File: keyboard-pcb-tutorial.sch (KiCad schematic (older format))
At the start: 14 parts

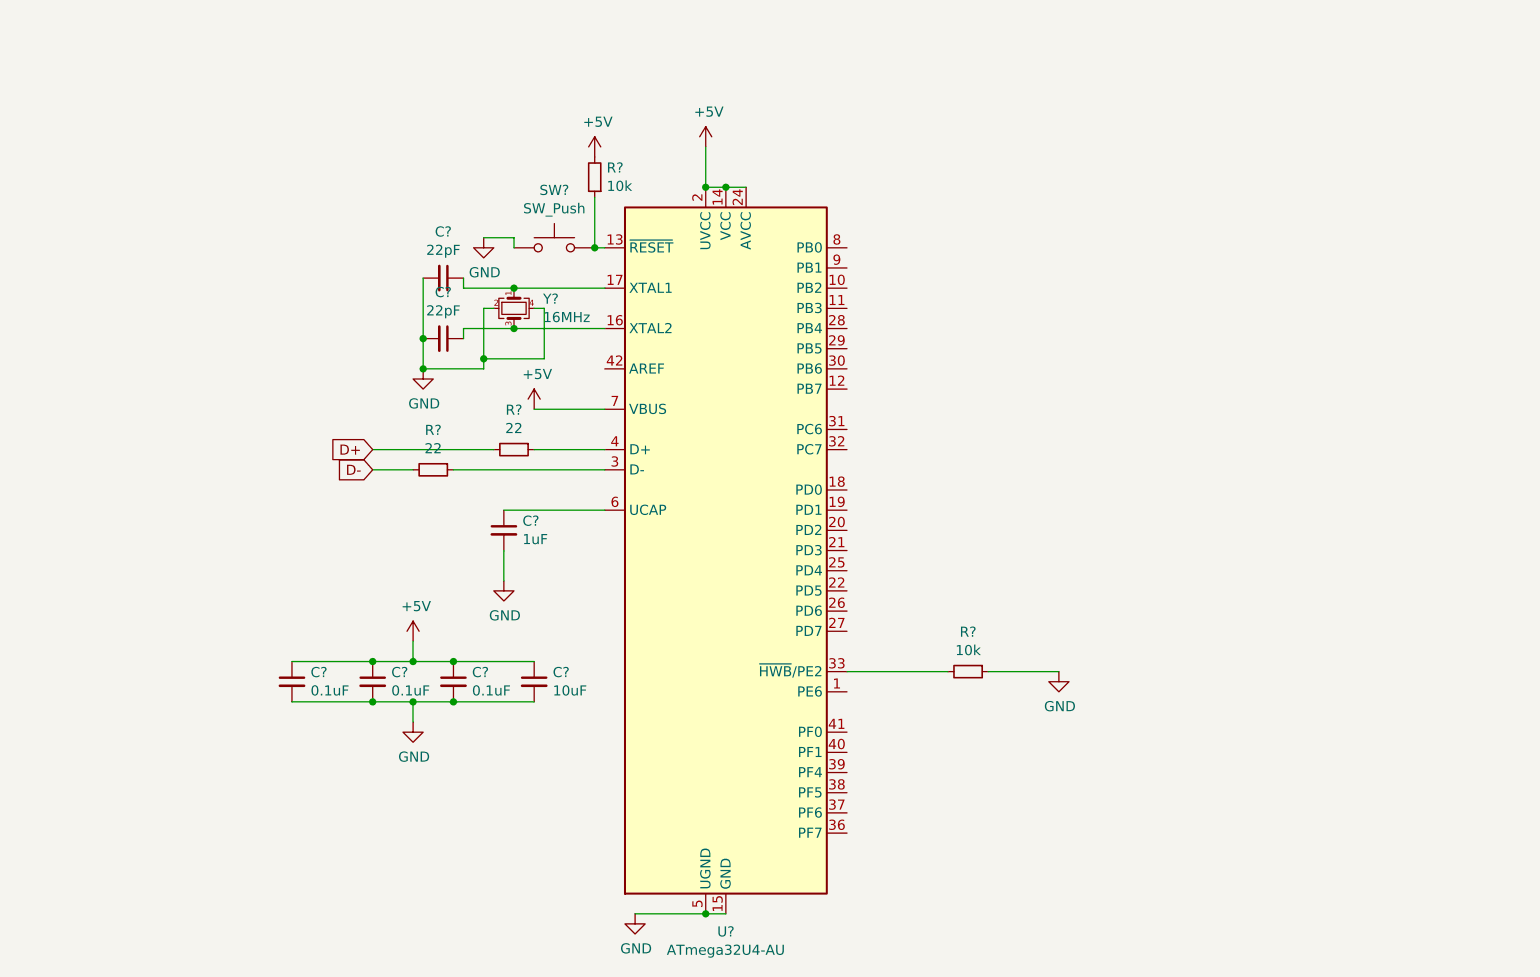
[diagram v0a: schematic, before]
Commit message: Added switch matrix schematic
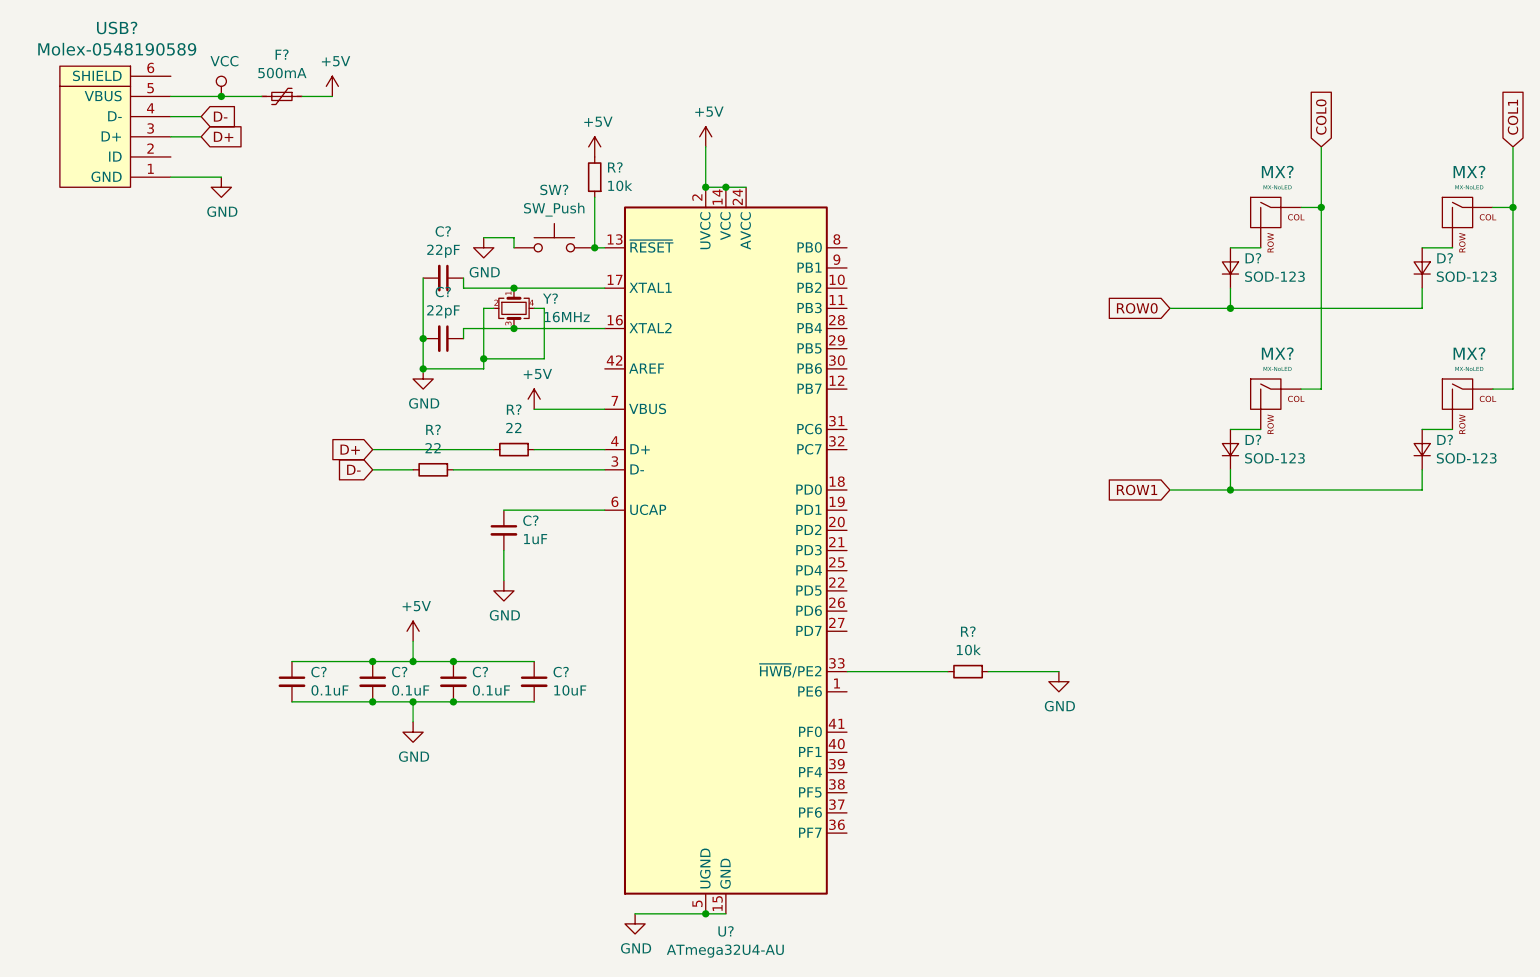
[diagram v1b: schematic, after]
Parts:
- added D? (x4): SOD-123, symbol Device:D_Small
- added F?: 500mA, symbol Device:Polyfuse_Small
- added MX? (x4): MX-NoLED, symbol MX_Alps_Hybrid:MX-NoLED
- added USB?: Molex-0548190589, symbol random-keyboard-parts:Molex-0548190589
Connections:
- net +5V: now also F?.1
- net D+: now also USB?.3 (D+)
- net D-: now also USB?.4 (D-)
- net GND: now also USB?.1 (GND)
- new net: D?.2 (A), MX?.2 (ROW) (x4)
- new net COL0: MX?.1 (COL), MX?.1 (COL)
- new net COL1: MX?.1 (COL), MX?.1 (COL)
- new net ROW0: D?.1 (K), D?.1 (K)
- new net ROW1: D?.1 (K), D?.1 (K)
- new net VCC: F?.2, USB?.5 (VBUS)
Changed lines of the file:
@@
 EESchema Schematic File Version 4
+LIBS:keyboard-pcb-tutorial-cache
 EELAYER 30 0
 EELAYER END
@@
 Text GLabel 2250 2800 0    50   Input ~ 0
 D-
+$Comp
+L random-keyboard-parts:Molex-0548190589 USB?
+U 1 1 601927A4
+P 950 1150
+F 0 "USB?" V 1487 1117 60  0000 C CNN
+F 1 "Molex-0548190589" V 1381 1117 60  0000 C CNN
+F 2 "" H 950 1150 60  0001 C CNN
+F 3 "" H 950 1150 60  0001 C CNN
+	1    950  1150
+	0    -1   -1   0
+$EndComp
+$Comp
+L power:+5V #PWR?
+U 1 1 60196CE8
+P 2050 950
+F 0 "#PWR?" H 2050 800 50  0001 C CNN
+F 1 "+5V" H 2065 1123 50  0000 C CNN
+F 2 "" H 2050 950 50  0001 C CNN
+F 3 "" H 2050 950 50  0001 C CNN
+	1    2050 950
+	1    0    0    -1
+$EndComp
+$Comp
+L power:GND #PWR?
+U 1 1 60197560
+P 1500 1350
+F 0 "#PWR?" H 1500 1100 50  0001 C CNN
+F 1 "GND" H 1505 1177 50  0000 C CNN
+F 2 "" H 1500 1350 50  0001 C CNN
+F 3 "" H 1500 1350 50  0001 C CNN
+	1    1500 1350
+	1    0    0    -1
+$EndComp
+Wire Wire Line
+	1250 1350 1500 1350
+Text GLabel 1400 1150 2    50   Input ~ 0
+D+
+Text GLabel 1400 1050 2    50   Input ~ 0
+D-
+Wire Wire Line
+	1250 1050 1400 1050
+Wire Wire Line
+	1400 1150 1250 1150
+$Comp
+L power:VCC #PWR?
+U 1 1 6019AFE7
+P 1500 950
+F 0 "#PWR?" H 1500 800 50  0001 C CNN
+F 1 "VCC" H 1517 1123 50  0000 C CNN
+F 2 "" H 1500 950 50  0001 C CNN
+F 3 "" H 1500 950 50  0001 C CNN
+	1    1500 950
+	1    0    0    -1
+$EndComp
+Wire Wire Line
+	1250 950  1500 950
+$Comp
+L Device:Polyfuse_Small F?
+U 1 1 6019CF5D
+P 1800 950
+F 0 "F?" V 1595 950 50  0000 C CNN
+F 1 "500mA" V 1686 950 50  0000 C CNN
+F 2 "" H 1850 750 50  0001 L CNN
+F 3 "~" H 1800 950 50  0001 C CNN
+	1    1800 950
+	0    1    1    0
+$EndComp
+Wire Wire Line
+	1500 950  1700 950
+Connection ~ 1500 950
+Wire Wire Line
+	1900 950  2050 950
+$Comp
+L MX_Alps_Hybrid:MX-NoLED MX?
+U 1 1 6019FDFB
+P 6700 1550
+F 0 "MX?" H 6733 1773 60  0000 C CNN
+F 1 "MX-NoLED" H 6733 1699 20  0000 C CNN
+F 2 "" H 6075 1525 60  0001 C CNN
+F 3 "" H 6075 1525 60  0001 C CNN
+	1    6700 1550
+	1    0    0    -1
+$EndComp
+$Comp
+L MX_Alps_Hybrid:MX-NoLED MX?
+U 1 1 601A13FC
+P 7650 1550
+F 0 "MX?" H 7683 1773 60  0000 C CNN
+F 1 "MX-NoLED" H 7683 1699 20  0000 C CNN
+F 2 "" H 7025 1525 60  0001 C CNN
+F 3 "" H 7025 1525 60  0001 C CNN
+	1    7650 1550
+	1    0    0    -1
+$EndComp
+$Comp
+L MX_Alps_Hybrid:MX-NoLED MX?
+U 1 1 601A1B0A
+P 6700 2450
+F 0 "MX?" H 6733 2673 60  0000 C CNN
+F 1 "MX-NoLED" H 6733 2599 20  0000 C CNN
+F 2 "" H 6075 2425 60  0001 C CNN
+F 3 "" H 6075 2425 60  0001 C CNN
+	1    6700 2450
+	1    0    0    -1
+$EndComp
+$Comp
+L MX_Alps_Hybrid:MX-NoLED MX?
+U 1 1 601A2B2D
+P 7650 2450
+F 0 "MX?" H 7683 2673 60  0000 C CNN
+F 1 "MX-NoLED" H 7683 2599 20  0000 C CNN
+F 2 "" H 7025 2425 60  0001 C CNN
+F 3 "" H 7025 2425 60  0001 C CNN
+	1    7650 2450
+	1    0    0    -1
+$EndComp
+$Comp
+L Device:D_Small D?
+U 1 1 601A3C44
+P 6500 1800
+F 0 "D?" V 6546 1732 50  0000 R CNN
+F 1 "SOD-123" V 6455 1732 50  0000 R CNN
+F 2 "" V 6500 1800 50  0001 C CNN
+F 3 "~" V 6500 1800 50  0001 C CNN
+	1    6500 1800
+	0    -1   -1   0
+$EndComp
+$Comp
+L Device:D_Small D?
+U 1 1 601A6318
+P 6500 2700
+F 0 "D?" V 6546 2632 50  0000 R CNN
+F 1 "SOD-123" V 6455 2632 50  0000 R CNN
+F 2 "" V 6500 2700 50  0001 C CNN
+F 3 "~" V 6500 2700 50  0001 C CNN
+	1    6500 2700
+	0    -1   -1   0
+$EndComp
+$Comp
+L Device:D_Small D?
+U 1 1 601A7160
+P 7450 2700
+F 0 "D?" V 7496 2632 50  0000 R CNN
+F 1 "SOD-123" V 7405 2632 50  0000 R CNN
+F 2 "" V 7450 2700 50  0001 C CNN
+F 3 "~" V 7450 2700 50  0001 C CNN
+	1    7450 2700
+	0    -1   -1   0
+$EndComp
+$Comp
+L Device:D_Small D?
+U 1 1 601A83EF
+P 7450 1800
+F 0 "D?" V 7496 1732 50  0000 R CNN
+F 1 "SOD-123" V 7405 1732 50  0000 R CNN
+F 2 "" V 7450 1800 50  0001 C CNN
+F 3 "~" V 7450 1800 50  0001 C CNN
+	1    7450 1800
+	0    -1   -1   0
+$EndComp
+Wire Wire Line
+	6500 1700 6650 1700
+Wire Wire Line
+	6500 2600 6650 2600
+Wire Wire Line
+	7450 2600 7600 2600
+Wire Wire Line
+	7450 1700 7600 1700
+Wire Wire Line
+	6850 1500 6950 1500
+Wire Wire Line
+	6950 1500 6950 2400
+Wire Wire Line
+	6950 2400 6850 2400
+Wire Wire Line
+	6950 1500 6950 1200
+Connection ~ 6950 1500
+Wire Wire Line
+	7800 2400 7900 2400
+Wire Wire Line
+	7900 2400 7900 1500
+Wire Wire Line
+	7800 1500 7900 1500
+Connection ~ 7900 1500
+Wire Wire Line
+	7900 1500 7900 1200
+Wire Wire Line
+	6500 1900 6500 2000
+Wire Wire Line
+	6500 2800 6500 2900
+Wire Wire Line
+	7450 2800 7450 2900
+Wire Wire Line
+	7450 2900 6500 2900
+Connection ~ 6500 2900
+Wire Wire Line
+	6500 2900 6200 2900
+Wire Wire Line
+	6200 2000 6500 2000
+Wire Wire Line
+	7450 2000 7450 1900
+Connection ~ 6500 2000
+Wire Wire Line
+	6500 2000 7450 2000
+Text GLabel 6200 2000 0    50   Input ~ 0
+ROW0
+Text GLabel 6200 2900 0    50   Input ~ 0
+ROW1
+Text GLabel 6950 1200 1    50   Input ~ 0
+COL0
+Text GLabel 7900 1200 1    50   Input ~ 0
+COL1
 $EndSCHEMATC

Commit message: Added footprints
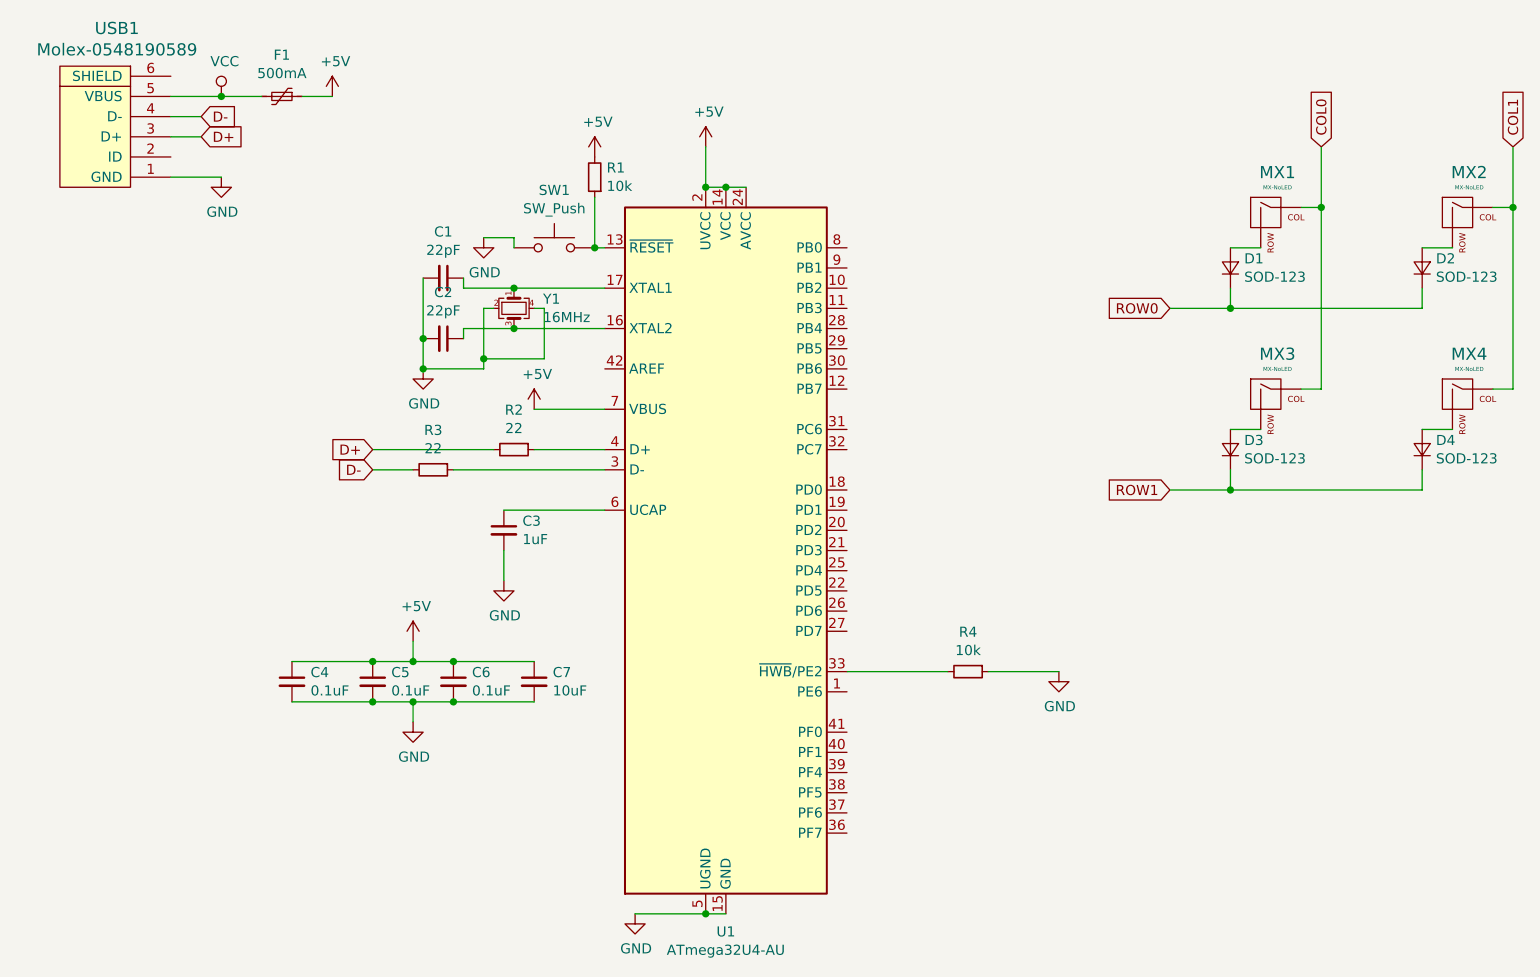
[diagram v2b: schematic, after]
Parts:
- C1, C2, C3, C4, C5, C6, C7: renamed from C?; footprint (none) -> Capacitor_SMD:C_0805_2012Metric
- D1, D2, D3, D4: renamed from D?; footprint (none) -> Diode_SMD:D_SOD-123
- F1: renamed from F?; footprint (none) -> Fuse:Fuse_1206_3216Metric
- R1, R2, R3, R4: renamed from R?; footprint (none) -> Resistor_SMD:R_0805_2012Metric
- SW1: renamed from SW?; footprint (none) -> random-keyboard-parts:SKQG-1155865
- USB1: renamed from USB?; footprint (none) -> random-keyboard-parts:Molex-0548190589
- Y1: renamed from Y?; footprint (none) -> Crystal:Crystal_SMD_3225-4Pin_3.2x2.5mm
- gave numbers to parts that had none: 5

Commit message: added basic pcb layout
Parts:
- MX1, MX2, MX3, MX4: footprint (none) -> MX_Alps_Hybrid:MX-1U-NoLED
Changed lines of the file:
@@
 F 0 "MX1" H 6733 1773 60  0000 C CNN
 F 1 "MX-NoLED" H 6733 1699 20  0000 C CNN
-F 2 "" H 6075 1525 60  0001 C CNN
+F 2 "MX_Alps_Hybrid:MX-1U-NoLED" H 6075 1525 60  0001 C CNN
 F 3 "" H 6075 1525 60  0001 C CNN
 	1    6700 1550
@@
 F 0 "MX2" H 7683 1773 60  0000 C CNN
 F 1 "MX-NoLED" H 7683 1699 20  0000 C CNN
-F 2 "" H 7025 1525 60  0001 C CNN
+F 2 "MX_Alps_Hybrid:MX-1U-NoLED" H 7025 1525 60  0001 C CNN
 F 3 "" H 7025 1525 60  0001 C CNN
 	1    7650 1550
@@
 F 0 "MX3" H 6733 2673 60  0000 C CNN
 F 1 "MX-NoLED" H 6733 2599 20  0000 C CNN
-F 2 "" H 6075 2425 60  0001 C CNN
+F 2 "MX_Alps_Hybrid:MX-1U-NoLED" H 6075 2425 60  0001 C CNN
 F 3 "" H 6075 2425 60  0001 C CNN
 	1    6700 2450
@@
 F 0 "MX4" H 7683 2673 60  0000 C CNN
 F 1 "MX-NoLED" H 7683 2599 20  0000 C CNN
-F 2 "" H 7025 2425 60  0001 C CNN
+F 2 "MX_Alps_Hybrid:MX-1U-NoLED" H 7025 2425 60  0001 C CNN
 F 3 "" H 7025 2425 60  0001 C CNN
 	1    7650 2450

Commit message: Finished routing
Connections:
- net COL0: now also U1.29 (PB5)
- net COL1: now also U1.28 (PB4)
- net ROW0: now also U1.27 (PD7)
- net ROW1: now also U1.30 (PB6)
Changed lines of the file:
@@
 Text GLabel 7900 1200 1    50   Input ~ 0
 COL1
+Text GLabel 4600 3600 2    50   Input ~ 0
+ROW0
+Text GLabel 4600 2300 2    50   Input ~ 0
+ROW1
+Text GLabel 4600 2200 2    50   Input ~ 0
+COL0
+Text GLabel 4600 2100 2    50   Input ~ 0
+COL1
 $EndSCHEMATC
